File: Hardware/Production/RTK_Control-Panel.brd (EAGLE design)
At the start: 171.8 x 115.8 mm, 409 parts, among them J3 MICRO-SD-PUSH-PUSH-EXT-PIN, J4 Vertical Qwiic Connector, J9 MAGJACK-POE, U1 ESP32-WROVER-IE, U10 POE_PSU-DP990X, U11 MCP6021T, U12 AP7361C-33, U13 MCP6021T, U14 BP2G1+_POWER_SPLITTER, U15 USB251XB, U16 SN74AVC4T774PW, U17 URB2405YMD-15WR3, U2 CH340C, U3 XC6222B331MR-G, U4 U-BLOX_ZED-F9P, U5 U-BLOX_NEO-D9S-00B, U6 XC6222B331MR-G, U7 W5500, U8 LARA-R6001, U9 74LVC4066D_QUAD_BILATERAL_SWI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, Y1 25MHz, Y2 24MHz

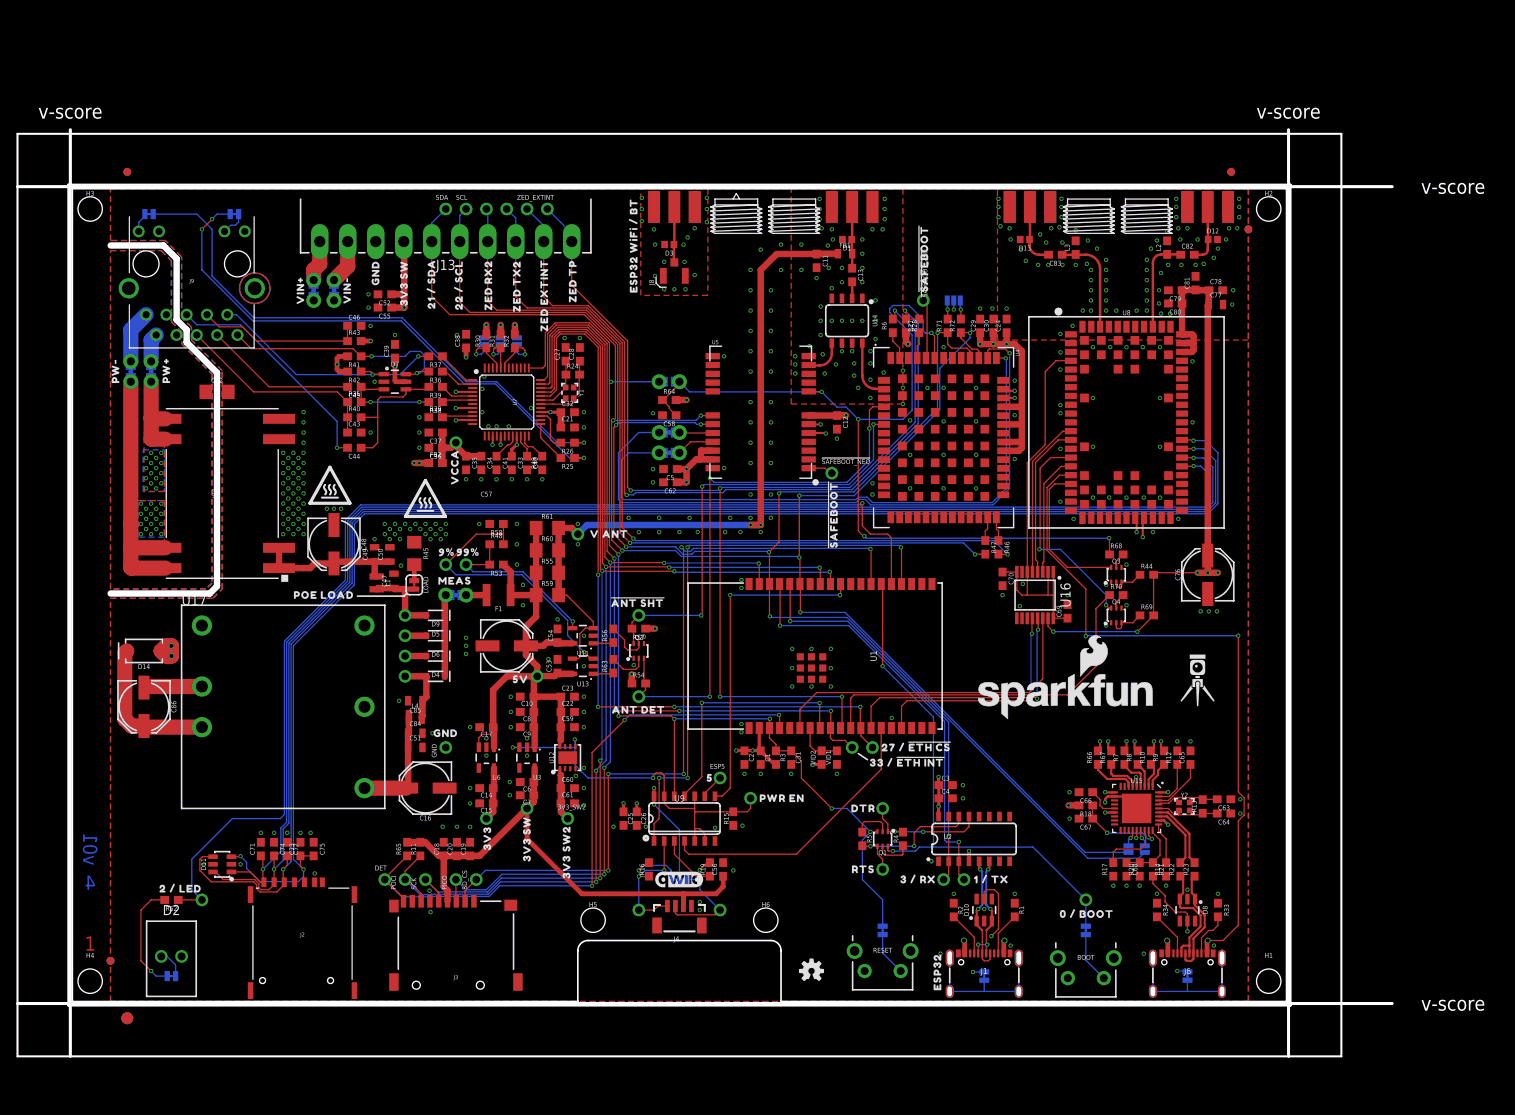
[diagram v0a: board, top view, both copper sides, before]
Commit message: Add Route-Out gaps on panel
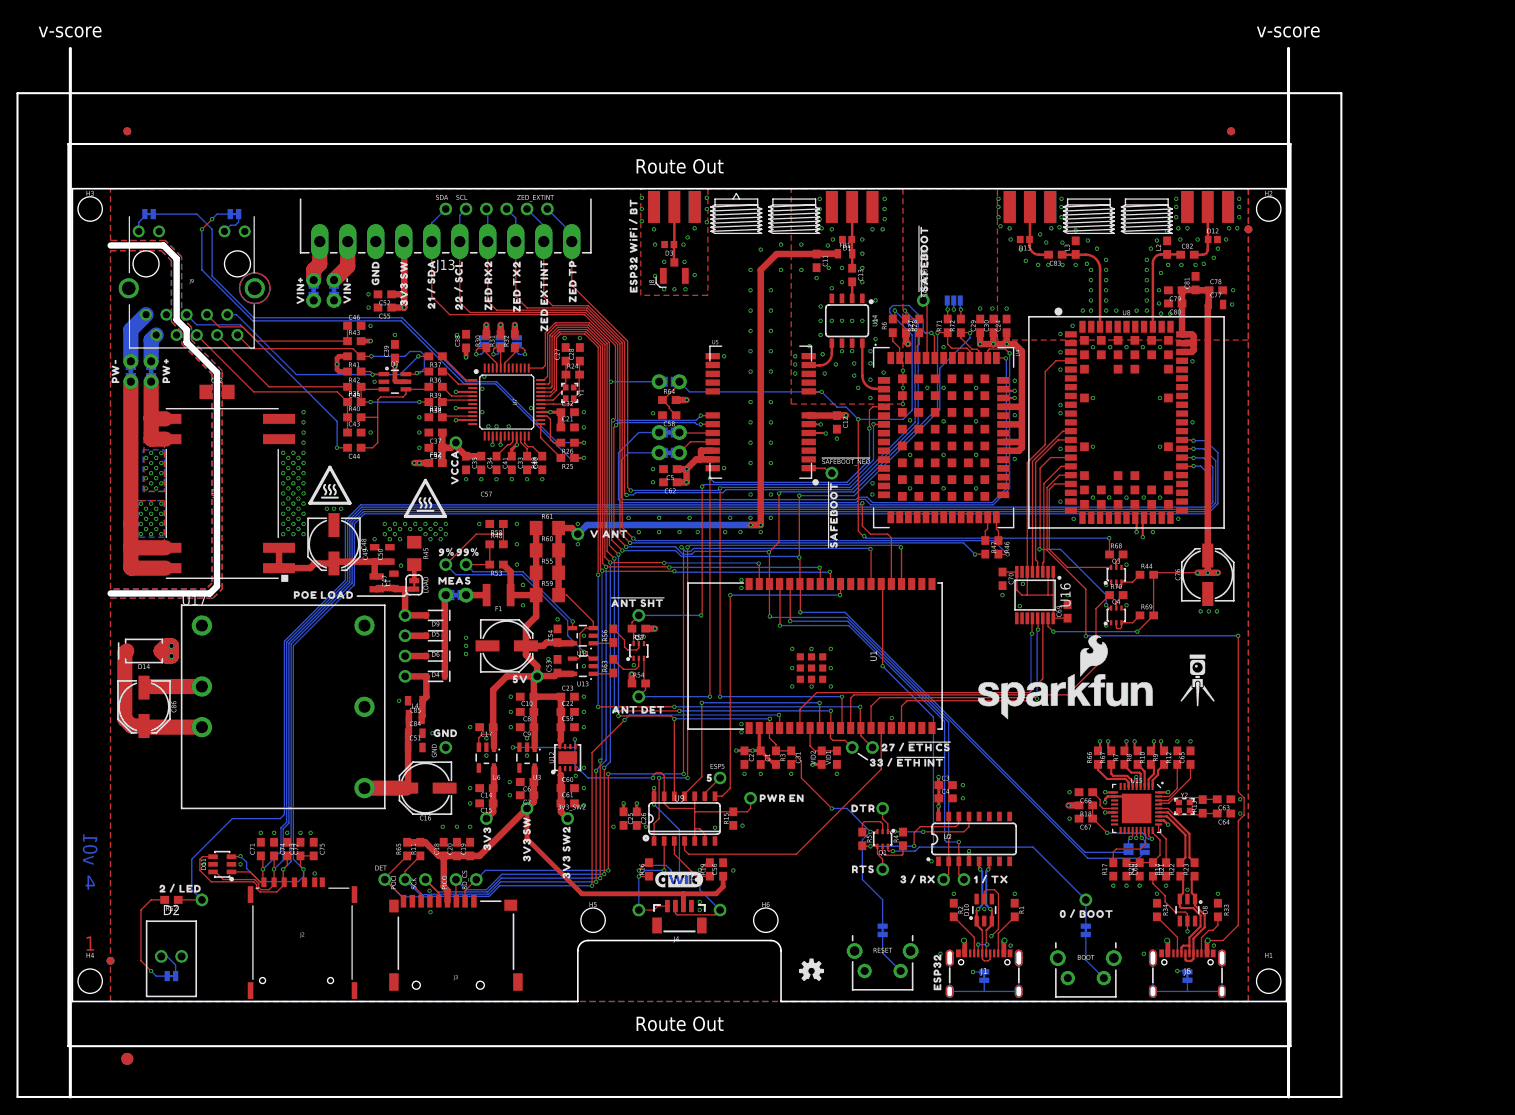
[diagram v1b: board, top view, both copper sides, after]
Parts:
- moved E$5 5.08 mm to (6.86, -7.18)
- moved E$6 5.08 mm to (6.86, -7.18)
- moved E$1 5.08 mm to (6.86, 108.8)
- moved E$2 5.08 mm to (6.86, 108.8)
- moved E$3 5.08 mm to (144.8, 108.8)
- moved E$4 5.08 mm to (144.8, 108.8)
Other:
- board size 171.8 x 115.8 mm -> 165.5 x 131.1 mm
- board text added: "Route Out"
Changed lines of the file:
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@@
 <vertex x="38.9255" y="60.071"/>
 </polygon>
-<wire x1="-0.254" y1="-6.858" x2="-0.254" y2="108.966" width="0.381" layer="46"/>
-<text x="-0.254" y="111.252" size="1.778" layer="46" ratio="15" align="center">v-score</text>
-<wire x1="152.019" y1="-6.858" x2="152.019" y2="108.966" width="0.381" layer="46"/>
-<text x="152.019" y="111.252" size="1.778" layer="46" ratio="15" align="center">v-score</text>
-<wire x1="-6.858" y1="-0.254" x2="164.973" y2="-0.254" width="0.381" layer="46"/>
-<text x="172.593" y="-0.254" size="1.778" layer="46" ratio="15" align="center">v-score</text>
-<wire x1="-6.858" y1="101.854" x2="164.973" y2="101.854" width="0.381" layer="46"/>
-<text x="172.593" y="101.854" size="1.778" layer="46" ratio="15" align="center">v-score</text>
-<wire x1="-0.508" y1="-0.508" x2="152.273" y2="-0.508" width="0.254" layer="20"/>
-<wire x1="158.623" y1="-6.858" x2="-6.858" y2="-6.858" width="0.254" layer="20"/>
-<wire x1="158.623" y1="108.458" x2="158.623" y2="-6.858" width="0.254" layer="20"/>
-<wire x1="152.273" y1="-0.508" x2="152.273" y2="102.108" width="0.254" layer="20"/>
-<wire x1="-6.858" y1="108.458" x2="158.623" y2="108.458" width="0.254" layer="20"/>
-<wire x1="152.273" y1="102.108" x2="-0.508" y2="102.108" width="0.254" layer="20"/>
-<wire x1="-0.508" y1="102.108" x2="-0.508" y2="-0.508" width="0.254" layer="20"/>
-<wire x1="-6.858" y1="-6.858" x2="-6.858" y2="108.458" width="0.254" layer="20"/>
+<text x="75.8825" y="-2.794" size="1.778" layer="20" ratio="15" align="center">Route Out</text>
+<text x="75.8825" y="104.394" size="1.778" layer="20" ratio="15" align="center">Route Out</text>
+<wire x1="-0.254" y1="-11.938" x2="-0.254" y2="119.126" width="0.381" layer="46"/>
+<text x="-0.254" y="121.412" size="1.778" layer="46" ratio="15" align="center">v-score</text>
+<wire x1="152.019" y1="-11.938" x2="152.019" y2="119.126" width="0.381" layer="46"/>
+<text x="152.019" y="121.412" size="1.778" layer="46" ratio="15" align="center">v-score</text>
+<wire x1="-0.508" y1="-5.588" x2="152.273" y2="-5.588" width="0.254" layer="20"/>
+<wire x1="158.623" y1="-11.938" x2="-6.858" y2="-11.938" width="0.254" layer="20"/>
+<wire x1="158.623" y1="113.538" x2="158.623" y2="-11.938" width="0.254" layer="20"/>
+<wire x1="152.273" y1="-5.588" x2="152.273" y2="107.188" width="0.254" layer="20"/>
+<wire x1="-6.858" y1="113.538" x2="158.623" y2="113.538" width="0.254" layer="20"/>
+<wire x1="152.273" y1="107.188" x2="-0.508" y2="107.188" width="0.254" layer="20"/>
+<wire x1="-0.508" y1="107.188" x2="-0.508" y2="-5.588" width="0.254" layer="20"/>
+<wire x1="-6.858" y1="-11.938" x2="-6.858" y2="113.538" width="0.254" layer="20"/>
 </plain>
 <attributes>
@@
 <element name="U$79" library="output" package="UART14" value="" x="74.6125" y="72.898" smashed="yes" rot="MR0"/>
 <element name="U$89" library="output" package="4_#_#SD_CS#15" value="" x="50.4825" y="10.922" smashed="yes" rot="MR270"/>
-<element name="E$1" library="SparkFun-Aesthetics" package="FIDUCIAL-1X2" value="" x="6.858" y="103.6955" smashed="yes"/>
-<element name="E$2" library="SparkFun-Aesthetics" package="FIDUCIAL-1X2" value="" x="6.858" y="103.6955" smashed="yes" rot="MR0"/>
-<element name="E$3" library="SparkFun-Aesthetics" package="FIDUCIAL-1X2" value="" x="144.8435" y="103.6955" smashed="yes"/>
-<element name="E$4" library="SparkFun-Aesthetics" package="FIDUCIAL-1X2" value="" x="144.8435" y="103.6955" smashed="yes" rot="MR0"/>
-<element name="E$5" library="SparkFun-Retired" package="FIDUCIAL-1.5X3" value="" x="6.858" y="-2.0955" smashed="yes"/>
-<element name="E$6" library="SparkFun-Retired" package="FIDUCIAL-1.5X3" value="" x="6.858" y="-2.0955" smashed="yes" rot="MR0"/>
+<element name="E$1" library="SparkFun-Aesthetics" package="FIDUCIAL-1X2" value="" x="6.858" y="108.7755" smashed="yes"/>
+<element name="E$2" library="SparkFun-Aesthetics" package="FIDUCIAL-1X2" value="" x="6.858" y="108.7755" smashed="yes" rot="MR0"/>
+<element name="E$3" library="SparkFun-Aesthetics" package="FIDUCIAL-1X2" value="" x="144.8435" y="108.7755" smashed="yes"/>
+<element name="E$4" library="SparkFun-Aesthetics" package="FIDUCIAL-1X2" value="" x="144.8435" y="108.7755" smashed="yes" rot="MR0"/>
+<element name="E$5" library="SparkFun-Retired" package="FIDUCIAL-1.5X3" value="" x="6.858" y="-7.1755" smashed="yes"/>
+<element name="E$6" library="SparkFun-Retired" package="FIDUCIAL-1.5X3" value="" x="6.858" y="-7.1755" smashed="yes" rot="MR0"/>
 </elements>
 <signals>

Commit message: Update RTK_Control-Panel.brd
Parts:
- U15: value USB251XB -> USB251XB_USB2514B; device USB251xB:QFN-36 -> SparkFun-IC-Special-Function:QFN-36
- U17: value URB2405YMD-15WR3 -> URB2405YMD
- U8: value LARA-R6001 -> LARA-R6001D
- moved U17 0.32 mm to (26.7, 36.8)
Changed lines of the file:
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@@
 <element name="U1" library="SparkFun-RF" package="ESP32-WROVER-E/IE" value="ESP32-WROVER-IE" x="92.3925" y="43.18" smashed="yes" rot="R180">
 <attribute name="NAME" x="100.1525" y="43.18" size="0.8128" layer="25" rot="R270" align="center"/>
+<attribute name="PROD_ID" value="IC-19265" x="92.71" y="43.18" size="1.778" layer="27" rot="R180" display="off"/>
 <attribute name="VALUE" x="98.8825" y="43.18" size="0.8128" layer="27" rot="R270" align="center"/>
 </element>
@@
 <attribute name="VALUE" x="37.7825" y="13.462" size="0.6096" layer="27" font="vector" ratio="20"/>
 </element>
-<element name="U8" library="SparkFun-RF" package="LARA-LGA" value="LARA-R6001" x="131.7625" y="72.39" smashed="yes" rot="R270">
+<element name="U8" library="SparkFun-RF" package="LARA-LGA" value="LARA-R6001D" x="131.7625" y="72.39" smashed="yes" rot="R270">
 <attribute name="NAME" x="131.7625" y="85.79" size="0.6096" layer="25" font="vector" ratio="20" align="bottom-center"/>
-<attribute name="VALUE" x="131.7625" y="58.99" size="0.6096" layer="27" font="vector" ratio="20" rot="R180" align="bottom-center"/>
+<attribute name="PROD_ID" value="IC-16661" x="132.08" y="72.39" size="1.778" layer="27" rot="R270" display="off"/>
+<attribute name="VALUE" value="LARA-R6001D" x="132.08" y="58.99" size="0.6096" layer="27" font="vector" ratio="20" rot="R180" align="bottom-center"/>
 </element>
 <element name="C22" library="SparkFun-Capacitors" package="0603" value="2.2uF" x="61.9125" y="36.195" smashed="yes">
@@
 <attribute name="VALUE" x="139.0015" y="23.284" size="0.6096" layer="27" ratio="20" align="top-center"/>
 </element>
-<element name="U15" library="USB251xB" package="QFN-36" value="USB251XB" x="133.0325" y="24.13" smashed="yes" rot="R270">
+<element name="U15" library="SparkFun-IC-Special-Function" package="QFN-36" value="USB251XB_USB2514B" x="133.0325" y="24.13" smashed="yes" rot="R270">
 <attribute name="NAME" x="133.0325" y="27.305" size="0.6096" layer="25" font="vector" ratio="20" align="bottom-center"/>
 <attribute name="PROD_ID" value="IC-15827" x="129.2225" y="27.94" size="1.778" layer="27" ratio="15" rot="R270" display="off"/>
@@
 <element name="C86" library="SparkFun-Capacitors" package="PANASONIC_D" value="47UF" x="8.9535" y="36.83" smashed="yes" rot="R270">
 <attribute name="NAME" x="12.3825" y="36.83" size="0.6096" layer="25" font="vector" ratio="20" rot="R270" align="bottom-center"/>
+<attribute name="PROD_ID" value="CAP-10547" x="9.271" y="36.83" size="1.778" layer="27" rot="R270" display="off"/>
 <attribute name="VALUE" x="5.5245" y="36.83" size="0.6096" layer="27" font="vector" ratio="20" rot="R270" align="top-center"/>
 </element>
-<element name="U17" library="SparkFun-IC-Power" package="URB_YMD-15WR3" value="URB2405YMD-15WR3" x="26.3525" y="36.83" smashed="yes">
+<element name="U17" library="SparkFun-IC-Power" package="URB_YMD-15WR3" value="URB2405YMD" x="26.67" y="36.83" smashed="yes">
 <attribute name="NAME" x="13.6525" y="49.53" size="1.27" layer="25" font="vector"/>
-<attribute name="PROD_ID" value="" x="26.3525" y="36.83" size="1.778" layer="27" display="off"/>
-<attribute name="VALUE" x="13.6525" y="22.86" size="1.27" layer="27" font="vector"/>
+<attribute name="PROD_ID" value="COMP-19263" x="26.3525" y="36.83" size="1.778" layer="27" display="off"/>
+<attribute name="VALUE" value="URB2405YMD" x="13.6525" y="22.86" size="1.27" layer="27" font="vector"/>
 </element>
 <element name="I2C1" library="SparkFun-Jumpers" package="SMT-JUMPER_3_NO_SILK" package3d_urn="urn:adsk.eagle:package:39285/1" value="JUMPER-SMT_3_NO_SILK" x="110.1725" y="87.63" smashed="yes" rot="MR0">

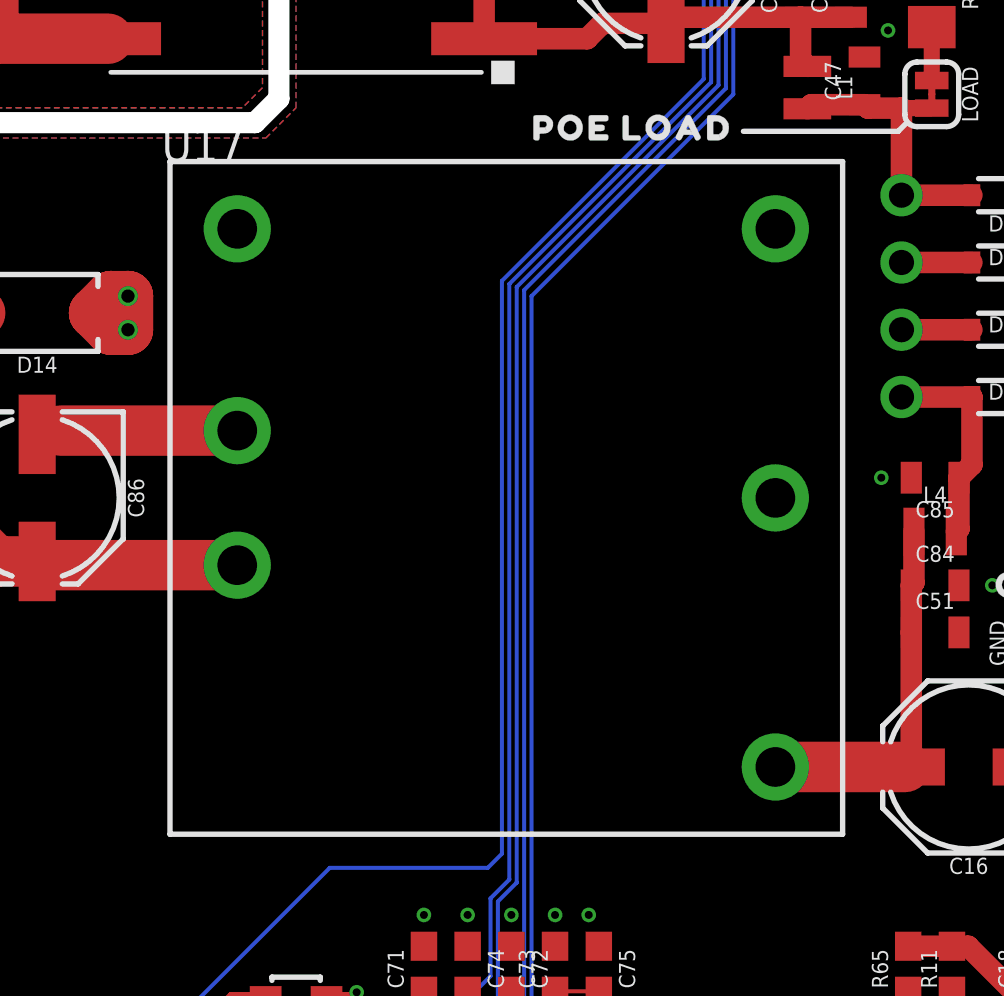
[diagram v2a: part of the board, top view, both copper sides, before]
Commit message: Update attribute positions
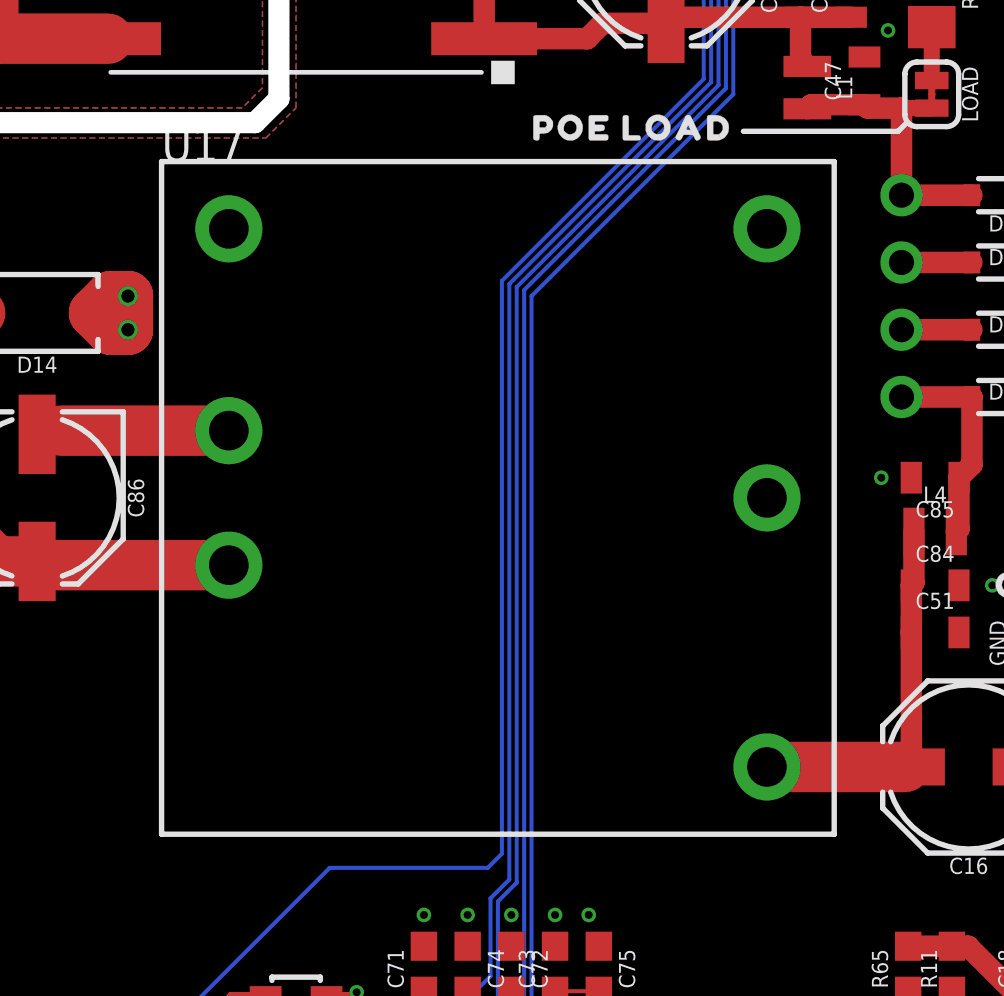
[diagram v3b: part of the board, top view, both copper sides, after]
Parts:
- moved U17 0.32 mm to (26.4, 36.8)
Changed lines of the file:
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@@
 <element name="U1" library="SparkFun-RF" package="ESP32-WROVER-E/IE" value="ESP32-WROVER-IE" x="92.3925" y="43.18" smashed="yes" rot="R180">
 <attribute name="NAME" x="100.1525" y="43.18" size="0.8128" layer="25" rot="R270" align="center"/>
-<attribute name="PROD_ID" value="IC-19265" x="92.71" y="43.18" size="1.778" layer="27" rot="R180" display="off"/>
+<attribute name="PROD_ID" value="IC-19265" x="92.3925" y="43.18" size="1.778" layer="27" rot="R180" display="off"/>
 <attribute name="VALUE" x="98.8825" y="43.18" size="0.8128" layer="27" rot="R270" align="center"/>
 </element>
@@
 <element name="U8" library="SparkFun-RF" package="LARA-LGA" value="LARA-R6001D" x="131.7625" y="72.39" smashed="yes" rot="R270">
 <attribute name="NAME" x="131.7625" y="85.79" size="0.6096" layer="25" font="vector" ratio="20" align="bottom-center"/>
-<attribute name="PROD_ID" value="IC-16661" x="132.08" y="72.39" size="1.778" layer="27" rot="R270" display="off"/>
-<attribute name="VALUE" value="LARA-R6001D" x="132.08" y="58.99" size="0.6096" layer="27" font="vector" ratio="20" rot="R180" align="bottom-center"/>
+<attribute name="PROD_ID" value="IC-16661" x="131.7625" y="72.39" size="1.778" layer="27" rot="R270" display="off"/>
+<attribute name="VALUE" value="LARA-R6001D" x="131.7625" y="58.99" size="0.6096" layer="27" font="vector" ratio="20" rot="R180" align="bottom-center"/>
 </element>
 <element name="C22" library="SparkFun-Capacitors" package="0603" value="2.2uF" x="61.9125" y="36.195" smashed="yes">
@@
 <element name="C86" library="SparkFun-Capacitors" package="PANASONIC_D" value="47UF" x="8.9535" y="36.83" smashed="yes" rot="R270">
 <attribute name="NAME" x="12.3825" y="36.83" size="0.6096" layer="25" font="vector" ratio="20" rot="R270" align="bottom-center"/>
-<attribute name="PROD_ID" value="CAP-10547" x="9.271" y="36.83" size="1.778" layer="27" rot="R270" display="off"/>
+<attribute name="PROD_ID" value="CAP-10547" x="8.9535" y="36.83" size="1.778" layer="27" rot="R270" display="off"/>
 <attribute name="VALUE" x="5.5245" y="36.83" size="0.6096" layer="27" font="vector" ratio="20" rot="R270" align="top-center"/>
 </element>
-<element name="U17" library="SparkFun-IC-Power" package="URB_YMD-15WR3" value="URB2405YMD" x="26.67" y="36.83" smashed="yes">
+<element name="U17" library="SparkFun-IC-Power" package="URB_YMD-15WR3" value="URB2405YMD" x="26.3525" y="36.83" smashed="yes">
 <attribute name="NAME" x="13.6525" y="49.53" size="1.27" layer="25" font="vector"/>
 <attribute name="PROD_ID" value="COMP-19263" x="26.3525" y="36.83" size="1.778" layer="27" display="off"/>
